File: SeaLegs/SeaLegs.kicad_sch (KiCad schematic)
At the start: 0 parts

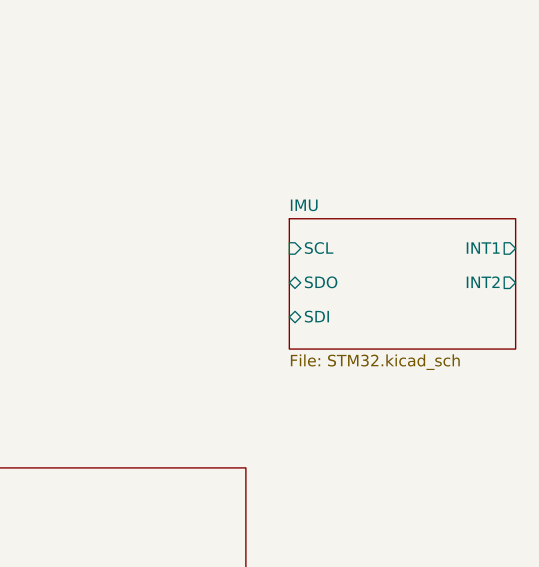
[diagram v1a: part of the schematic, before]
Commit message: Updated decision matrix
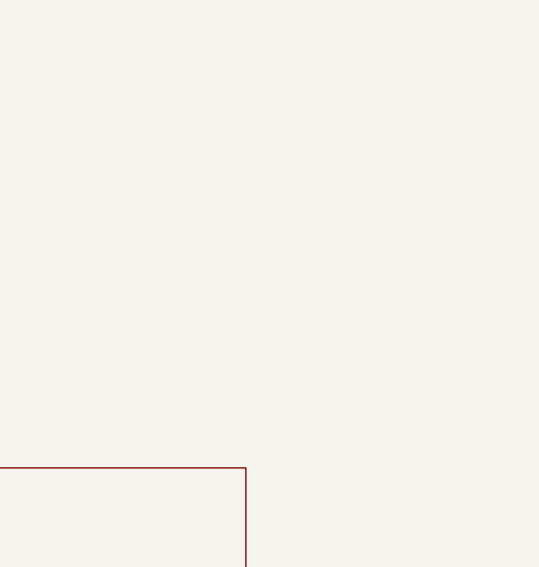
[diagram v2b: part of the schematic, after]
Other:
- removed sheet IMU
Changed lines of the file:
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@@
-	)
-	(sheet
-		(at 179.07 49.784)
-		(size 25.146 14.478)
-		(exclude_from_sim no)
-		(in_bom yes)
-		(on_board yes)
-		(dnp no)
-		(fields_autoplaced yes)
-		(stroke
-			(width 0.1524)
-			(type solid)
-		)
-		(fill
-			(color 0 0 194 0.25)
-		)
-		(property "Sheetname" "IMU"
-			(at 179.07 49.0724 0)
-			(show_name no)
-			(do_not_autoplace no)
-			(effects
-				(font
-					(size 1.27 1.27)
-				)
-				(justify left bottom)
-			)
-		)
-		(property "Sheetfile" "STM32.kicad_sch"
-			(at 179.07 64.8466 0)
-			(show_name no)
-			(do_not_autoplace no)
-			(effects
-				(font
-					(size 1.27 1.27)
-				)
-				(justify left top)
-			)
-		)
-		(pin "INT2" output
-			(at 204.216 56.896 0)
-			(effects
-				(font
-					(size 1.27 1.27)
-				)
-				(justify right)
-			)
-		)
-		(pin "SCL" input
-			(at 179.07 53.086 180)
-			(effects
-				(font
-					(size 1.27 1.27)
-				)
-				(justify left)
-			)
-		)
-		(pin "INT1" output
-			(at 204.216 53.086 0)
-			(effects
-				(font
-					(size 1.27 1.27)
-				)
-				(justify right)
-			)
-		)
-		(pin "SDO" bidirectional
-			(at 179.07 56.896 180)
-			(effects
-				(font
-					(size 1.27 1.27)
-				)
-				(justify left)
-			)
-		)
-		(pin "SDI" bidirectional
-			(at 179.07 60.706 180)
-			(effects
-				(font
-					(size 1.27 1.27)
-				)
-				(justify left)
-			)
-		)
-		(instances
-			(project "SeaLegs"
-				(path "/b358fa4f-8f13-49ea-bd67-d5db91173379"
-					(page "4")
-				)
-			)
-		)
 	)
 	(sheet
